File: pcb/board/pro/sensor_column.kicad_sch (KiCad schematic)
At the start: 4 parts, among them U210 CD74HC4067SM96

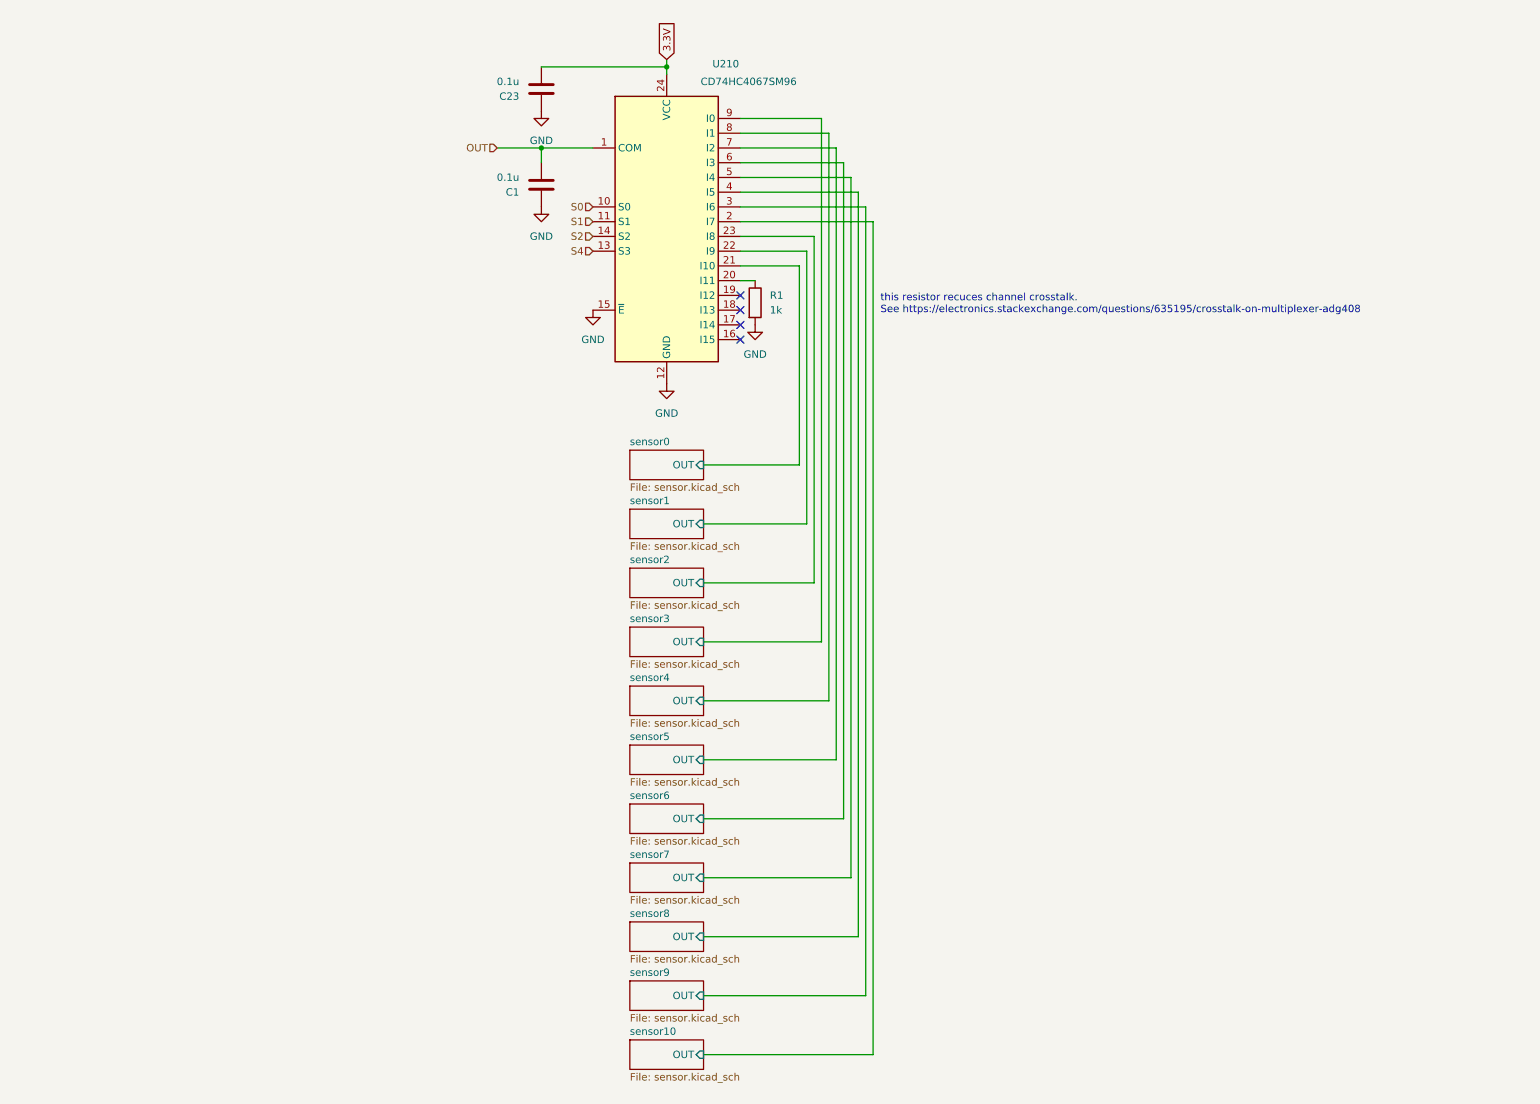
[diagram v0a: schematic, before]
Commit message: Update PCB with HSE oscillator, Footprint Mismatch fix and Rename project files to Wonkle (#36)
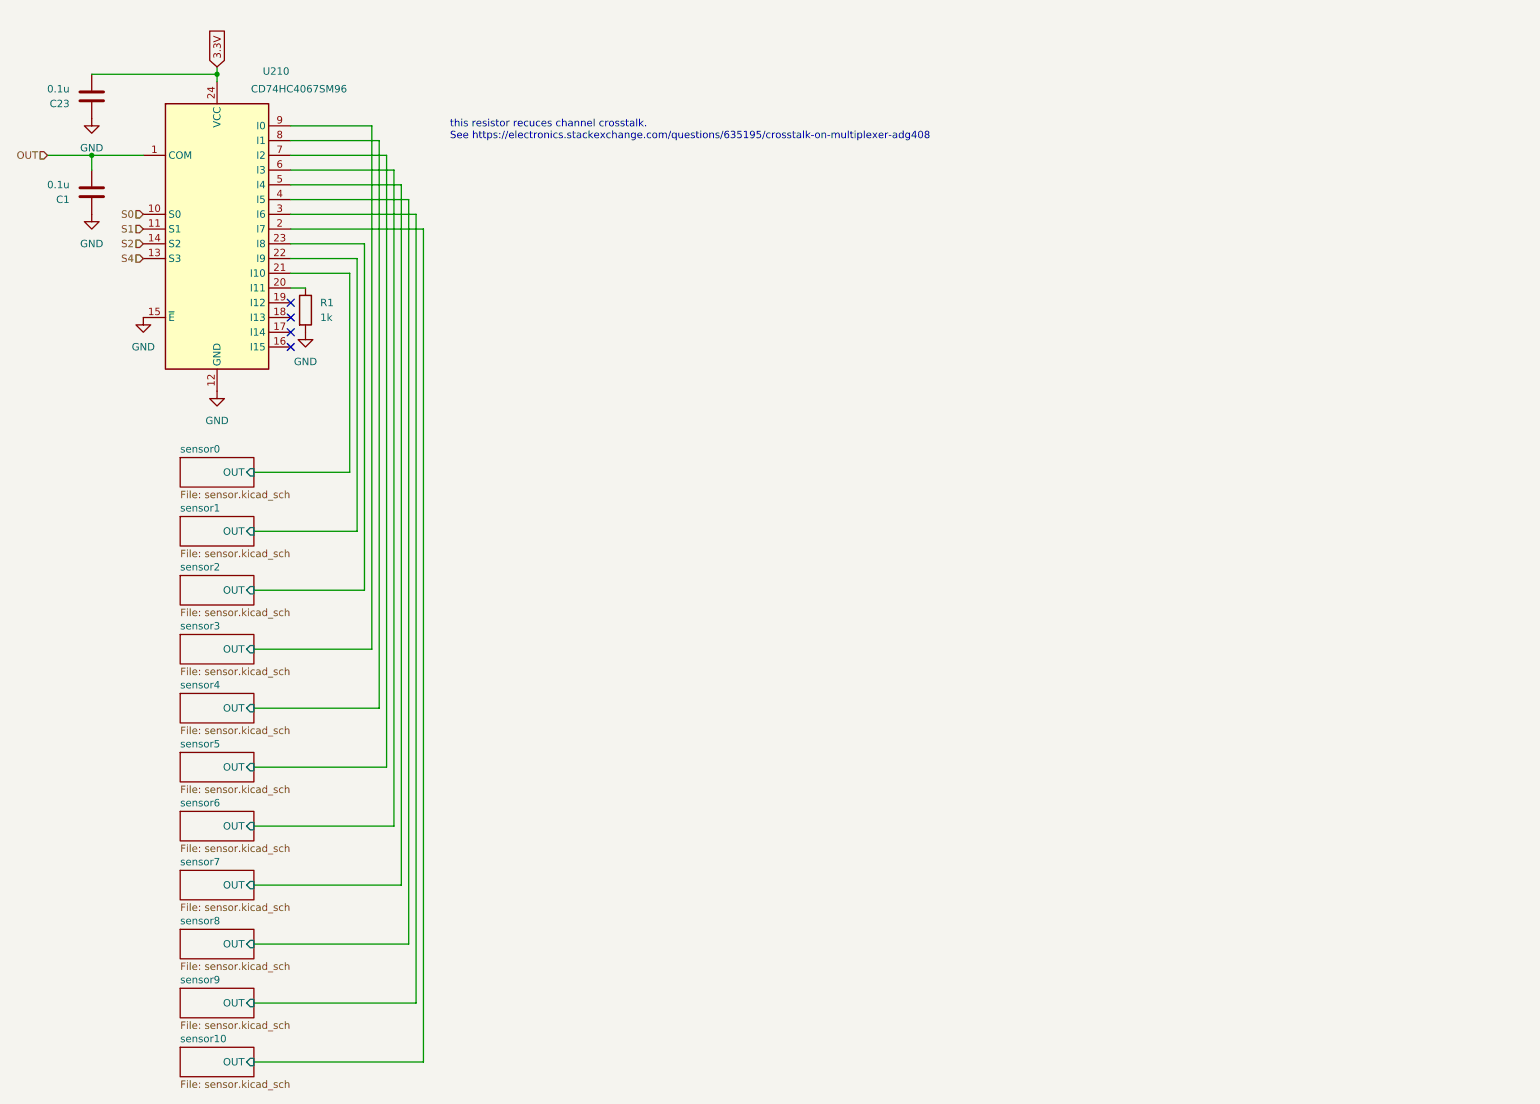
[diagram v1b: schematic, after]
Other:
- moved on the sheet: C1, C23, R1, U210
